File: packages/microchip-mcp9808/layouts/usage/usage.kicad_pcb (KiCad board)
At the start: 2 copper layers, 5 parts

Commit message: fix some more packages
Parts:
- C1: value 100nF ±10% 16V X7R -> {8.99999998509884e-08..1.1000000014901162e-07}F
- R1, R2, R3: value 10kΩ ±1% 62.5mW -> {10000.0±1.0%}Ω
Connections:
- net GND renamed lv
- net VCC renamed 7

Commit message: review tool updates
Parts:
- C1: value {8.99999998509884e-08..1.1000000014901162e-07}F -> 1.0000000000000001e-07F
- R1, R2, R3: value {10000.0±1.0%}Ω -> 10000.0Ω
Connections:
- net 7 renamed hv

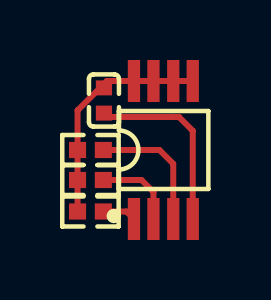
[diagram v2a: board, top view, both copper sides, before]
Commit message: remove all those other changes, just bosch baby
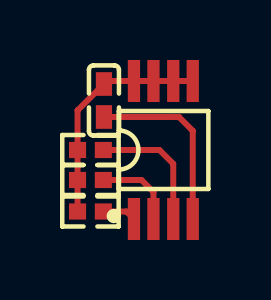
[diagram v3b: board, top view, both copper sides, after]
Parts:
- C1: value 1.0000000000000001e-07F -> 100nF ±10% 16V X7R
- R1, R2, R3: value 10000.0Ω -> 10kΩ ±1% 62.5mW
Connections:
- net hv renamed VCC
- net lv renamed GND
